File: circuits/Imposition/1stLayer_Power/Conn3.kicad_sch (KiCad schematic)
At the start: 9 parts, among them J9 Conn_01x08_MountingPin

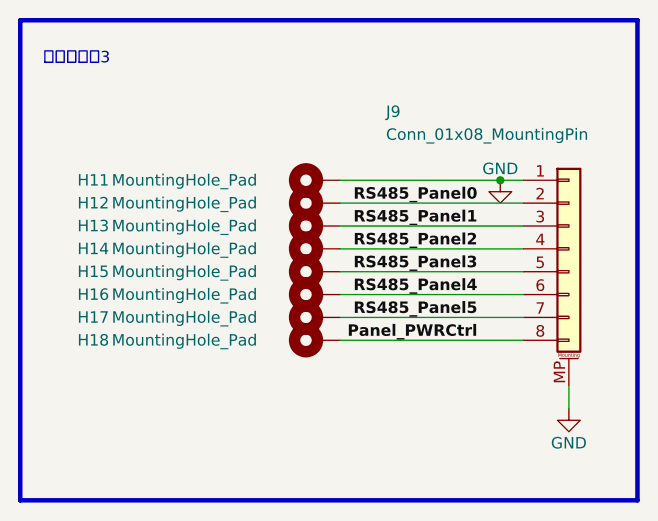
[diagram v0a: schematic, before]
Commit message: 発注_第一弾
Drive, 1stLayer_Power, 2ndLayer_3rdLayer
を発注
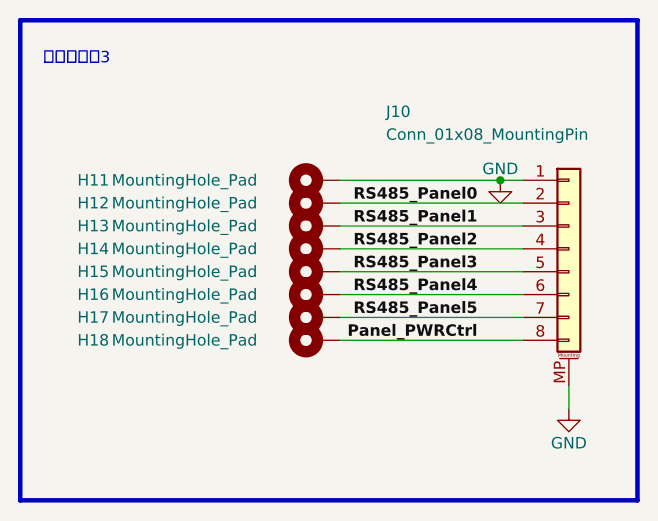
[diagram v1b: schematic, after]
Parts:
- renumbered J9 to J10
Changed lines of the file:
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@@
   (symbol (lib_id "Connector_Generic_MountingPin:Conn_01x08_MountingPin") (at 175.26 99.06 0) (unit 1)
     (in_bom yes) (on_board yes) (dnp no)
-    (property "Reference" "J9" (at 154.94 83.82 0)
+    (property "Reference" "J10" (at 154.94 83.82 0)
       (effects (font (size 1.27 1.27)) (justify left))
     )
@@
       (project "1stLayer_Power"
         (path "/599e2e4a-5379-461e-b684-22a177410a52/4a61e366-1cba-40f1-8aa2-f8a5f6651237"
-          (reference "J9") (unit 1)
+          (reference "J10") (unit 1)
         )
       )
